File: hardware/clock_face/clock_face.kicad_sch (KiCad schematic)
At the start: 0 parts

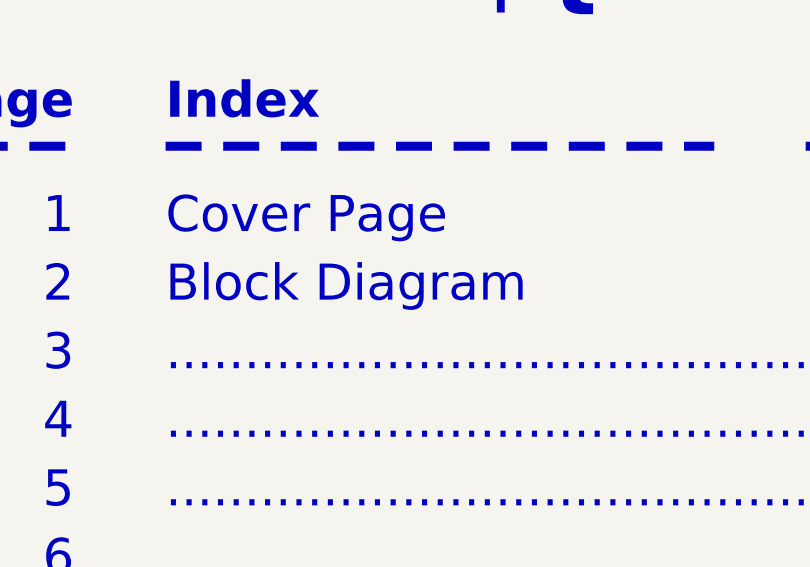
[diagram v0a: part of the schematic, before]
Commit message: Tweaking existing gerber files and schematics to comply with new project structure
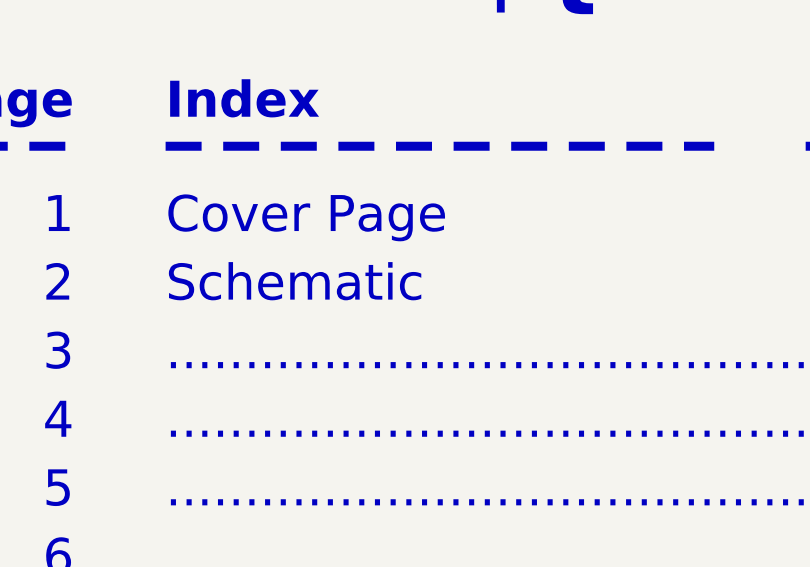
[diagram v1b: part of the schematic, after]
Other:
- note added: "Schematic"
- note removed: "Block Diagram"
